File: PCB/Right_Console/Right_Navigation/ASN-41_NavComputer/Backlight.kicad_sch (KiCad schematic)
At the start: 8 parts, among them J7 J_BACKLIGHT, J8 J_ARC51_PANEL_BL, Q1 AO3400A, Q2 AO3400A

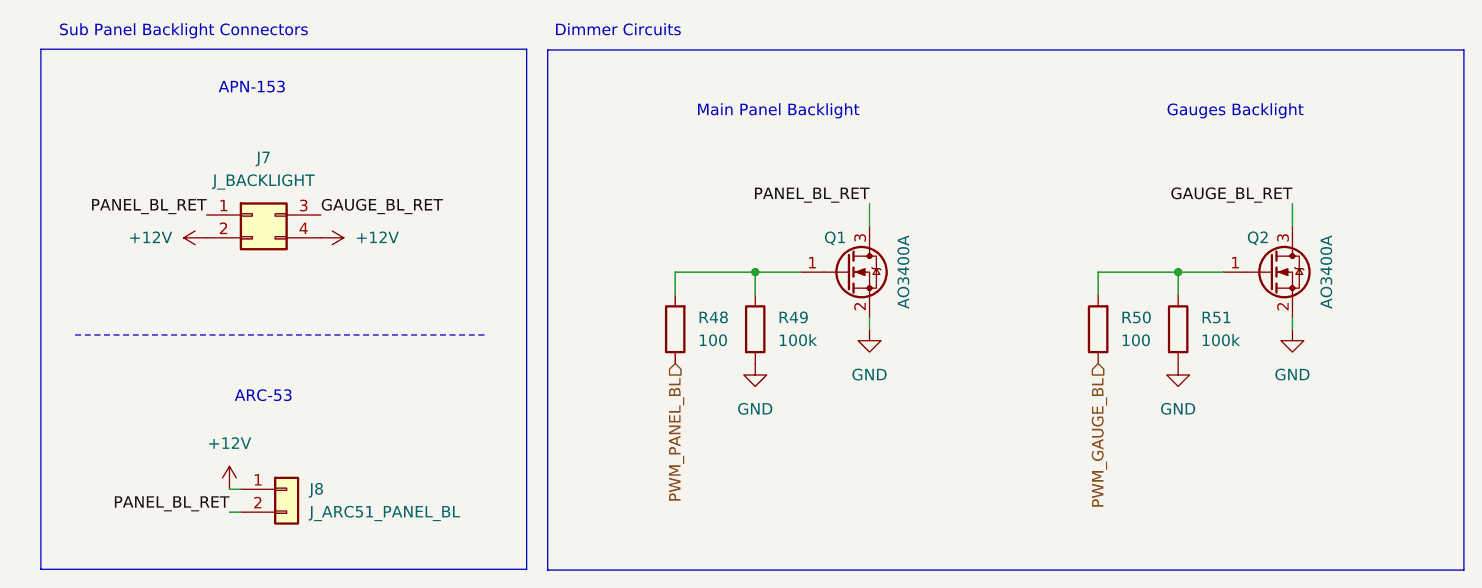
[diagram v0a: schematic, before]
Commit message: fix(pcb): Right_Nav harness-contract fixes — J7 5V, '165 spares, APN sync
Netlist-audit follow-ups on the ASN-41 host + APN-153 mate:
- J7 dual-zone backlight pin 4 -> +5V utility (standard dual-zone; was +12V)
- U12 '165 spare inputs D6/D7 (R46/R47) -> +3V3 pull-up (was GND) — matches
  the board's active-low scheme + all other inputs, restores wire-and-go
- APN-153: J4 backlight pin 4 -> +5V, aligning the mate to the host J7

Confirmed correct as-is (no change): J6/J1 I2C pin-8 +5V (trunk-sourced flex
for APN's 5V stepper/MEM) and J8 J_BL order (matches the fabbed PanelGroup_Base).
ERC: 0.
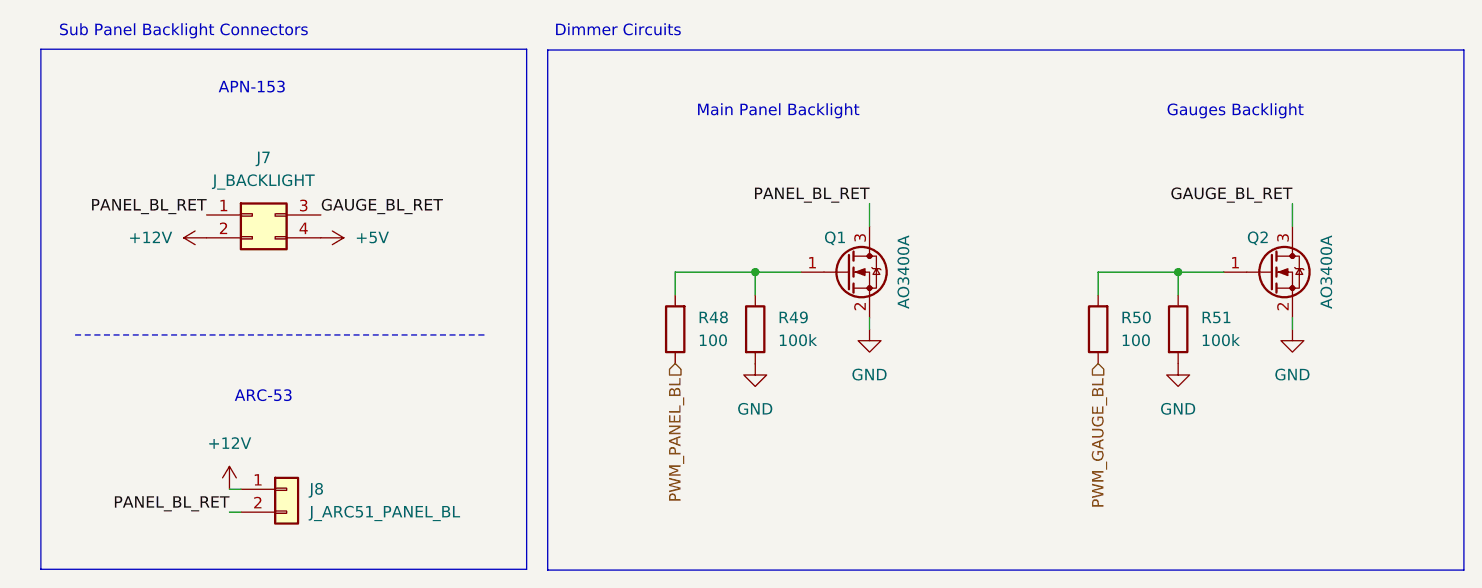
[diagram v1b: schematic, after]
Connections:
- net +12V: no longer J7.4 (Pin_4)
- new net +5V: J7.4 (Pin_4)
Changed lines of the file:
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@@
-	(symbol
-		(lib_id "power:+12V")
-		(at 46.99 158.75 270)
-		(unit 1)
-		(body_style 1)
-		(exclude_from_sim no)
-		(in_bom yes)
-		(on_board yes)
-		(in_pos_files yes)
-		(dnp no)
-		(fields_autoplaced yes)
-		(property "Reference" "#PWR0126"
-			(at 43.18 158.75 0)
-			(hide yes)
-			(show_name no)
-			(do_not_autoplace no)
-			(effects
-				(font
-					(size 1.27 1.27)
-				)
-			)
-		)
-		(property "Value" "+12V"
-			(at 50.8 158.7499 90)
-			(show_name no)
-			(do_not_autoplace no)
-			(effects
-				(font
-					(size 1.27 1.27)
-				)
-				(justify left)
-			)
-		)
-		(property "Footprint" ""
-			(at 46.99 158.75 0)
-			(hide yes)
-			(show_name no)
-			(do_not_autoplace no)
-			(effects
-				(font
-					(size 1.27 1.27)
-				)
-			)
-		)
-		(property "Datasheet" ""
-			(at 46.99 158.75 0)
-			(hide yes)
-			(show_name no)
-			(do_not_autoplace no)
-			(effects
-				(font
-					(size 1.27 1.27)
-				)
-			)
-		)
-		(property "Description" "Power symbol creates a global label with name \"+12V\""
-			(at 46.99 158.75 0)
-			(hide yes)
-			(show_name no)
-			(do_not_autoplace no)
-			(effects
-				(font
-					(size 1.27 1.27)
-				)
-			)
-		)
-		(pin "1"
-		)
-		(instances
-			(project "ASN-41_NavComputer"
-				(path "/44380fee-2d92-4c15-902c-f5cfd680baf1/9694bb82-0359-4efa-84e4-c5b38d300110"
-					(reference "#PWR0126")
-					(unit 1)
-				)
-			)
-		)
-	)
 	(symbol
 		(lib_id "power:+12V")
@@
 					(unit 1)
 				)
+			)
+		)
+	)
+	(symbol
+		(lib_id "power:+5V")
+		(at 46.99 158.75 270)
+		(unit 1)
+		(body_style 1)
+		(exclude_from_sim no)
+		(in_bom yes)
+		(on_board yes)
+		(in_pos_files yes)
+		(dnp no)
+		(fields_autoplaced yes)
+		(property "Reference" "#PWR0126"
+			(at 43.18 158.75 0)
+			(hide yes)
+			(show_name no)
+			(do_not_autoplace no)
+			(effects
+				(font
+					(size 1.27 1.27)
+				)
+			)
+		)
+		(property "Value" "+5V"
+			(at 50.8 158.7499 90)
+			(show_name no)
+			(do_not_autoplace no)
+			(effects
+				(font
+					(size 1.27 1.27)
+				)
+				(justify left)
+			)
+		)
+		(property "Footprint" ""
+			(at 46.99 158.75 0)
+			(hide yes)
+			(show_name no)
+			(do_not_autoplace no)
+			(effects
+				(font
+					(size 1.27 1.27)
+				)
+			)
+		)
+		(property "Datasheet" ""
+			(at 46.99 158.75 0)
+			(hide yes)
+			(show_name no)
+			(do_not_autoplace no)
+			(effects
+				(font
+					(size 1.27 1.27)
+				)
+			)
+		)
+		(property "Description" "Power symbol creates a global label with name \"+5V\""
+			(at 46.99 158.75 0)
+			(hide yes)
+			(show_name no)
+			(do_not_autoplace no)
+			(effects
+				(font
+					(size 1.27 1.27)
+				)
+			)
+		)
+		(pin "1"
+		)
+		(instances
+			(project "ASN-41_NavComputer"
+				(path "/44380fee-2d92-4c15-902c-f5cfd680baf1/9694bb82-0359-4efa-84e4-c5b38d300110"
+					(reference "#PWR0126")
+					(unit 1)
+				)

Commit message: fix(pcb): ASN-41 J8 backlight label typo ARC-53 -> ARC-51
Free-text label on the Backlight sheet only; symbol value J_ARC51_PANEL_BL
was already correct. Last remaining B2 cleanup item. ERC: 0.
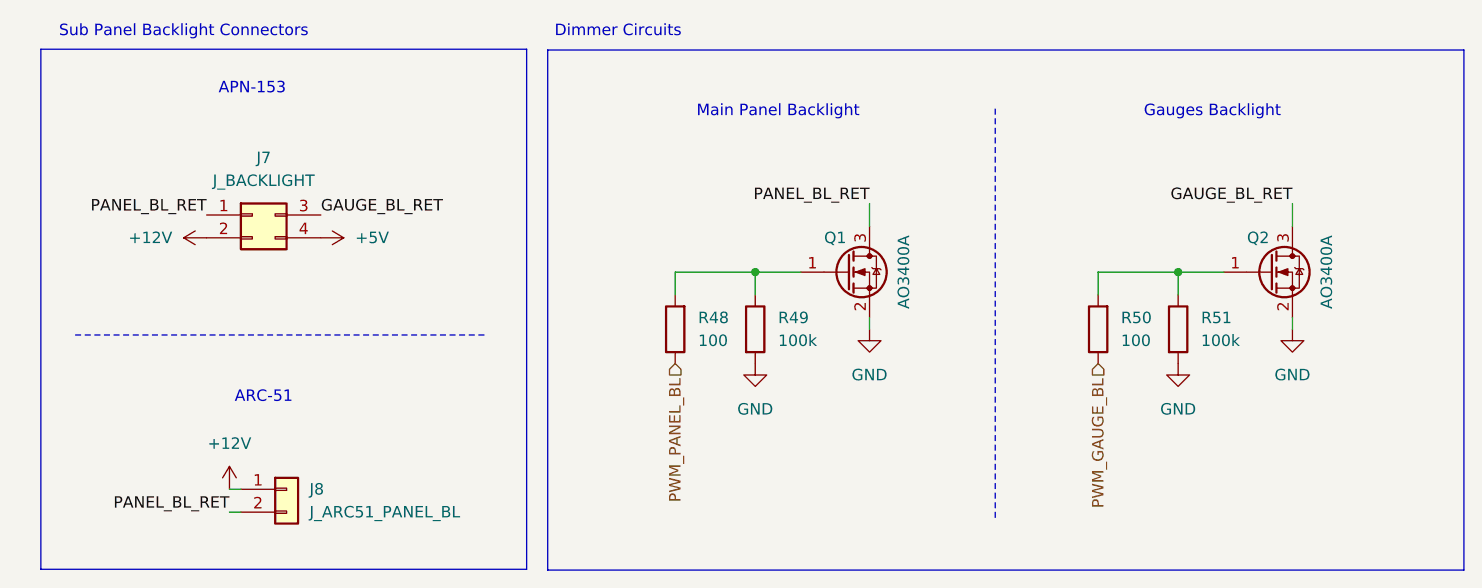
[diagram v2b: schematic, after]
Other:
- note added: "ARC-51"
- note removed: "ARC-53"
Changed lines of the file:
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@@
 	(text "Gauges Backlight"
 		(exclude_from_sim no)
-		(at 148.59 144.78 0)
+		(at 146.05 144.78 0)
 		(effects
 			(font
@@
 		)
 	)
-	(text "ARC-53"
+	(text "ARC-51"
 		(exclude_from_sim no)
 		(at 40.64 176.53 0)
@@
 		)
 	)
+	(polyline
+		(pts
+			(xy 121.92 189.865) (xy 121.92 144.145)
+		)
+		(stroke
+			(width 0)
+			(type dash)
+			(color 0 194 194 1)
+		)
+	)

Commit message: feat(pcb): label LCSC/tolerance/voltage across fleet boards (Right_Nav + PDU + base) (#235)
Populates **LCSC part number + tolerance + voltage** fields across all
six fleet boards, so each schematic drives an orderable BOM.

## Boards labeled (ERC 0/0 on all)
- **Right_Nav:** ASN-41, ARC-51A, APN-153
- **Power:** PDU
- **Base:** Gateway_Bridge, PanelGroup_Base

## What it does
- LCSC + tolerance + voltage on every assembled part, corrected to the
selected part (100nF 50V, resistors 1%, AMS1117 C6186→C347222, 10µF
split 25V/35V by +12V rail).
- Off-board panel controls (encoders, rotary switches, OLED, pot,
stepper, MEM button) left blank — connector-coupled, no assembly LCSC.
- Pin headers hand-soldered; RP2040-Zero left blank (module, sourced
separately).

## Design corrections captured here
- **PDU 1k series/anti-alias → 1%** (C110774 0.1% → C844939): precision
belongs only on the divider ratio resistors (33k/13k/10k); the series 1k
sit into high-Z ADC pins where 1% is identical. Drops the precision part
from the board.
- **DESIGN-NOTES:** records the 1k downgrade + the order-time shunt
upgrade (C346481 ±100ppm → C500740 ±25ppm, drop-in 2512).

## Not in this PR (follow-ups)
- Fleet component **standardization** (10µF-bulk→electrolytic,
consolidate to single 35V value, IPN convention) — separate pass.
- InvenTree backfill of the new SKUs.
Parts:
- J7: LCSC (none) -> C20608114
- J8: LCSC (none) -> C20608113
- Q1, Q2: Rating (none) -> 30V
- R48, R50: LCSC (none) -> C844936; Tolerance 5% -> 1%
- R49, R51: LCSC (none) -> C844935; Tolerance 5% -> 1%
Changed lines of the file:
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@@
 			)
 		)
-		(property "LCSC" ""
-			(at 0 0 0)
-			(hide yes)
-			(show_name no)
-			(do_not_autoplace no)
-			(effects
-				(font
-					(size 1.27 1.27)
-				)
-			)
-		)
-		(property "Tolerance" "5%"
+		(property "LCSC" "C844936"
+			(at 0 0 0)
+			(hide yes)
+			(show_name no)
+			(do_not_autoplace no)
+			(effects
+				(font
+					(size 1.27 1.27)
+				)
+			)
+		)
+		(property "Tolerance" "1%"
 			(at 0 0 0)
 			(hide yes)
@@
 			)
 		)
-		(property "Rating" ""
+		(property "Rating" "30V"
 			(at 0 0 0)
 			(hide yes)
@@
 			)
 		)
-		(property "LCSC" ""
+		(property "LCSC" "C20608114"
 			(at 0 0 0)
 			(hide yes)
@@
 			)
 		)
-		(property "LCSC" ""
-			(at 0 0 0)
-			(hide yes)
-			(show_name no)
-			(do_not_autoplace no)
-			(effects
-				(font
-					(size 1.27 1.27)
-				)
-			)
-		)
-		(property "Tolerance" "5%"
+		(property "LCSC" "C844935"
+			(at 0 0 0)
+			(hide yes)
+			(show_name no)
+			(do_not_autoplace no)
+			(effects
+				(font
+					(size 1.27 1.27)
+				)
+			)
+		)
+		(property "Tolerance" "1%"
 			(at 0 0 0)
 			(hide yes)
@@
 			)
 		)
-		(property "LCSC" ""
-			(at 0 0 0)
-			(hide yes)
-			(show_name no)
-			(do_not_autoplace no)
-			(effects
-				(font
-					(size 1.27 1.27)
-				)
-			)
-		)
-		(property "Tolerance" "5%"
+		(property "LCSC" "C844936"
+			(at 0 0 0)
+			(hide yes)
+			(show_name no)
+			(do_not_autoplace no)
+			(effects
+				(font
+					(size 1.27 1.27)
+				)
+			)
+		)
+		(property "Tolerance" "1%"
 			(at 0 0 0)
 			(hide yes)
@@
 			)
 		)
-		(property "LCSC" ""
-			(at 0 0 0)
-			(hide yes)
-			(show_name no)
-			(do_not_autoplace no)
-			(effects
-				(font
-					(size 1.27 1.27)
-				)
-			)
-		)
-		(property "Tolerance" "5%"
+		(property "LCSC" "C844935"
+			(at 0 0 0)
+			(hide yes)
+			(show_name no)
+			(do_not_autoplace no)
+			(effects
+				(font
+					(size 1.27 1.27)
+				)
+			)
+		)
+		(property "Tolerance" "1%"
 			(at 0 0 0)
 			(hide yes)
@@
 			)
 		)
-		(property "LCSC" ""
+		(property "LCSC" "C20608113"
 			(at 0 0 0)
 			(hide yes)
@@
 			)
 		)
-		(property "Rating" ""
-			(at 0 0 0)
-			(hide yes)
+		(property "Rating" "30V"
+			(at 0 0 0)
+			(hide yes)

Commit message: feat(pcb): add descriptive IPN field to all on-board symbols (#238 Phase 3) (#239)
Phase 3 of the IPN convention (#238): adds a stable, descriptive
**Internal Part Number** to every on-board symbol, co-equal with LCSC.
BOMs now anchor on a fixed identity; the LCSC can change with
availability without altering the part's identity.

## What changed
- **352 symbols** across all 6 boards (multi-sheet aware) get an `IPN`
field. **51 distinct IPNs.** ERC clean fleet-wide.
- **Off-board controls** (encoders/switches/pots/OLED/stepper — no
footprint, connector-coupled) get **no IPN**, per the standing off-board
exclusion. On-board modules (RP2040-ZERO) and the RESET tact switch
**do** get IPNs.
- `.gitignore`: FreeCAD backups (`*.FCBak`/`*.FCStd1`) + KiCad ERC/DRC
reports (`*-erc.rpt`/`*-drc.rpt`).

## Scheme (descriptive, locked in #238)
`RES-10K-1PCT-0805` · `CAP-CER-100NF-50V-0805` · `CAP-ELEC-22UF-16V-D4`
· `IC-STM32F103C8-LQFP` · `CONN-XH-8P` · `TVS-SMBJ12A-SMB` ·
`FUSE-HOLDER-BLADE-DIP4` · `SW-TACT-6MM` · `MOD-RP2040-ZERO`.

Resolved the 3 open encoding items: ferrite → `FB-600R-0805` (TDK
600Ω@100MHz), NTC → `NTC-10K-1206` (APV 10K), fuse holder (C19727305 is
a *holder*, not a fuse) → one `FUSE-HOLDER-BLADE-DIP4`.

## Not in this PR (later phases of #238)
- **Phase 2 — InvenTree:** set the IPN field + link SupplierParts incl
backorder alternates (one IPN → many LCSC). This is what actually
delivers the churn-proofing; needs reviewed InvenTree writes.
- **Phase 4 — order flow:** resolve IPN → in-stock LCSC at order time.

Refs #238.
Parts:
- J7: IPN (none) -> CONN-MF-4P
- J8: IPN (none) -> CONN-MF-2P
- Q1, Q2: IPN (none) -> Q-AO3400A-SOT23
- R48, R50: IPN (none) -> RES-100R-1PCT-0805
- R49, R51: IPN (none) -> RES-100K-1PCT-0805
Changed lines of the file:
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@@
+			)
+		)
+		(property "IPN" "RES-100R-1PCT-0805"
+			(at 86.36 168.91 0)
+			(hide yes)
+			(show_name no)
+			(do_not_autoplace no)
+			(effects
+				(font
+					(size 1.27 1.27)
+				)
 			)
 		)
@@
 		)
 		(property "Datasheet" ""
+			(at 154.94 162.56 0)
+			(hide yes)
+			(show_name no)
+			(do_not_autoplace no)
+			(effects
+				(font
+					(size 1.27 1.27)
+				)
+			)
+		)
+		(property "IPN" "Q-AO3400A-SOT23"
 			(at 154.94 162.56 0)
 			(hide yes)
@@
 			)
 		)
+		(property "IPN" "CONN-MF-4P"
+			(at 39.37 156.21 0)
+			(hide yes)
+			(show_name no)
+			(do_not_autoplace no)
+			(effects
+				(font
+					(size 1.27 1.27)
+				)
+			)
+		)
 		(property "Description" "Generic connector, double row, 02x02, top/bottom pin numbering scheme (row 1: 1...pins_per_row, row2: pins_per_row+1 ... num_pins), script generated (kicad-library-utils/schlib/autogen/connector/)"
 			(at 39.37 156.21 0)
@@
 			)
 		)
+		(property "IPN" "RES-100K-1PCT-0805"
+			(at 142.24 168.91 0)
+			(hide yes)
+			(show_name no)
+			(do_not_autoplace no)
+			(effects
+				(font
+					(size 1.27 1.27)
+				)
+			)
+		)
 		(property "Description" "Resistor"
 			(at 142.24 168.91 0)
@@
 			)
 		)
+		(property "IPN" "RES-100R-1PCT-0805"
+			(at 133.35 168.91 0)
+			(hide yes)
+			(show_name no)
+			(do_not_autoplace no)
+			(effects
+				(font
+					(size 1.27 1.27)
+				)
+			)
+		)
 		(property "Description" "Resistor"
 			(at 133.35 168.91 0)
@@
 			)
 		)
+		(property "IPN" "RES-100K-1PCT-0805"
+			(at 95.25 168.91 0)
+			(hide yes)
+			(show_name no)
+			(do_not_autoplace no)
+			(effects
+				(font
+					(size 1.27 1.27)
+				)
+			)
+		)
 		(property "Description" "Resistor"
 			(at 95.25 168.91 0)
@@
 			)
 		)
+		(property "IPN" "CONN-MF-2P"
+			(at 43.18 186.69 0)
+			(hide yes)
+			(show_name no)
+			(do_not_autoplace no)
+			(effects
+				(font
+					(size 1.27 1.27)
+				)
+			)
+		)
 		(property "Description" "Generic connector, single row, 01x02, script generated (kicad-library-utils/schlib/autogen/connector/)"
 			(at 43.18 186.69 0)
@@
 			(at 107.95 162.56 0)
 			(hide yes)
+			(show_name no)
+			(do_not_autoplace no)
+			(effects
+				(font
+					(size 1.27 1.27)
+				)
+			)
+		)
+		(property "IPN" "Q-AO3400A-SOT23"
+			(at 107.95 162.56 0)
+			(hide yes)

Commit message: refactor(pcb): genericize backlight FET symbol (IRLML2502 -> Q_NMOS_GSD)
The custom symbol was part-named IRLML2502, but the fitted part is the
AO3400A (30V, per the #232 backlight-FET standard) applied via a
per-instance Value/IPN override. Rename the shared symbol to a generic
N-FET donor so the name no longer implies a specific part: identity lives
in the instance Value + IPN (IPN convention), the symbol is just the
SOT-23 GSD footprint/pinout.

- OpenSkyhawk.kicad_sym: symbol IRLML2502 -> Q_NMOS_GSD; scrub the
  IRLML2502-specific Value/Description/Datasheet (was "20V ... Vgsth
  0.3-0.7V" + Infineon link) to a generic SOT-23 N-FET description.
- PanelGroup_Base + ASN-41_NavComputer: retarget the two FET instances'
  lib_id. Instance Value stays AO3400A; footprint (SOT-23) and pins
  (1/2/3 GSD) unchanged -> no reroute.
- Armament_MCU left on IRLML2502 (board being retired).

ERC clean on both live boards (kicad-cli sch erc, 0 violations).
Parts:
- Q1, Q2: symbol OpenSkyhawk:IRLML2502 -> OpenSkyhawk:Q_NMOS_GSD
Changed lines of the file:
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@@
 	)
 	(symbol
-		(lib_id "OpenSkyhawk:IRLML2502")
+		(lib_id "OpenSkyhawk:Q_NMOS_GSD")
 		(at 154.94 162.56 0)
 		(unit 1)
@@
 	)
 	(symbol
-		(lib_id "OpenSkyhawk:IRLML2502")
+		(lib_id "OpenSkyhawk:Q_NMOS_GSD")
 		(at 107.95 162.56 0)
 		(unit 1)
